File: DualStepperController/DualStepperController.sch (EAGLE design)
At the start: 14 parts

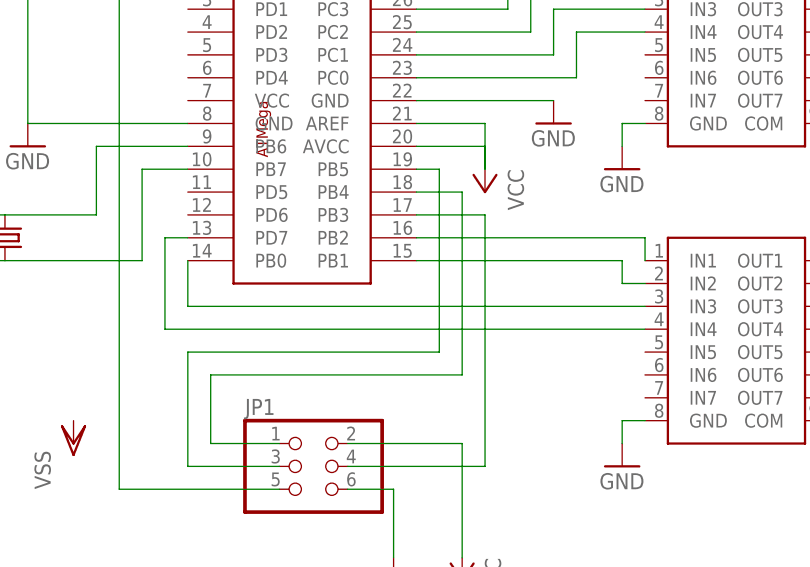
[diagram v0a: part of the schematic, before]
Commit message: Add mounting holes.
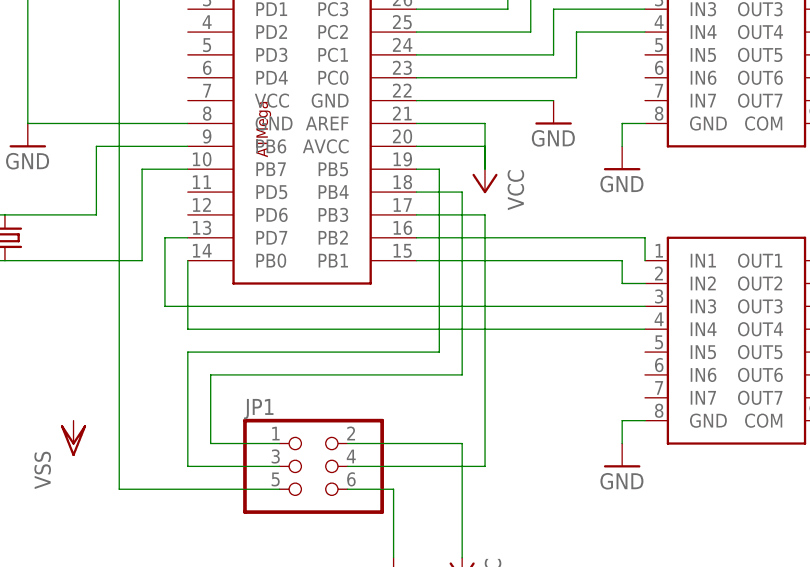
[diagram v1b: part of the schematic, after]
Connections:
- net N$24: now also U$3.IN4; no longer U$3.IN3
- net N$25: now also U$3.IN3; no longer U$3.IN4
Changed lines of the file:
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@@
 <grid distance="0.1" unitdist="inch" unit="inch" style="lines" multiple="1" display="no" altdistance="0.01" altunitdist="inch" altunit="inch"/>
 <layers>
-<layer number="1" name="Top" color="4" fill="1" visible="yes" active="no"/>
-<layer number="16" name="Bottom" color="1" fill="1" visible="yes" active="no"/>
-<layer number="17" name="Pads" color="2" fill="1" visible="yes" active="no"/>
-<layer number="18" name="Vias" color="2" fill="1" visible="yes" active="no"/>
-<layer number="19" name="Unrouted" color="6" fill="1" visible="yes" active="no"/>
-<layer number="20" name="Dimension" color="15" fill="1" visible="yes" active="no"/>
-<layer number="21" name="tPlace" color="7" fill="1" visible="yes" active="no"/>
-<layer number="22" name="bPlace" color="7" fill="1" visible="yes" active="no"/>
-<layer number="23" name="tOrigins" color="15" fill="1" visible="yes" active="no"/>
-<layer number="24" name="bOrigins" color="15" fill="1" visible="yes" active="no"/>
-<layer number="25" name="tNames" color="7" fill="1" visible="yes" active="no"/>
-<layer number="26" name="bNames" color="7" fill="1" visible="yes" active="no"/>
-<layer number="27" name="tValues" color="7" fill="1" visible="yes" active="no"/>
-<layer number="28" name="bValues" color="7" fill="1" visible="yes" active="no"/>
+<layer number="1" name="Top" color="4" fill="1" visible="no" active="no"/>
+<layer number="16" name="Bottom" color="1" fill="1" visible="no" active="no"/>
+<layer number="17" name="Pads" color="2" fill="1" visible="no" active="no"/>
+<layer number="18" name="Vias" color="2" fill="1" visible="no" active="no"/>
+<layer number="19" name="Unrouted" color="6" fill="1" visible="no" active="no"/>
+<layer number="20" name="Dimension" color="15" fill="1" visible="no" active="no"/>
+<layer number="21" name="tPlace" color="7" fill="1" visible="no" active="no"/>
+<layer number="22" name="bPlace" color="7" fill="1" visible="no" active="no"/>
+<layer number="23" name="tOrigins" color="15" fill="1" visible="no" active="no"/>
+<layer number="24" name="bOrigins" color="15" fill="1" visible="no" active="no"/>
+<layer number="25" name="tNames" color="7" fill="1" visible="no" active="no"/>
+<layer number="26" name="bNames" color="7" fill="1" visible="no" active="no"/>
+<layer number="27" name="tValues" color="7" fill="1" visible="no" active="no"/>
+<layer number="28" name="bValues" color="7" fill="1" visible="no" active="no"/>
 <layer number="29" name="tStop" color="7" fill="3" visible="no" active="no"/>
 <layer number="30" name="bStop" color="7" fill="6" visible="no" active="no"/>
@@
 <layer number="35" name="tGlue" color="7" fill="4" visible="no" active="no"/>
 <layer number="36" name="bGlue" color="7" fill="5" visible="no" active="no"/>
-<layer number="37" name="tTest" color="7" fill="1" visible="yes" active="no"/>
-<layer number="38" name="bTest" color="7" fill="1" visible="yes" active="no"/>
+<layer number="37" name="tTest" color="7" fill="1" visible="no" active="no"/>
+<layer number="38" name="bTest" color="7" fill="1" visible="no" active="no"/>
 <layer number="39" name="tKeepout" color="4" fill="11" visible="no" active="no"/>
 <layer number="40" name="bKeepout" color="1" fill="11" visible="no" active="no"/>
@@
 <layer number="44" name="Drills" color="7" fill="1" visible="no" active="no"/>
 <layer number="45" name="Holes" color="7" fill="1" visible="no" active="no"/>
-<layer number="46" name="Milling" color="3" fill="1" visible="yes" active="no"/>
-<layer number="47" name="Measures" color="7" fill="1" visible="yes" active="no"/>
-<layer number="48" name="Document" color="7" fill="1" visible="yes" active="no"/>
-<layer number="49" name="Reference" color="7" fill="1" visible="yes" active="no"/>
-<layer number="51" name="tDocu" color="7" fill="1" visible="yes" active="no"/>
-<layer number="52" name="bDocu" color="7" fill="1" visible="yes" active="no"/>
+<layer number="46" name="Milling" color="3" fill="1" visible="no" active="no"/>
+<layer number="47" name="Measures" color="7" fill="1" visible="no" active="no"/>
+<layer number="48" name="Document" color="7" fill="1" visible="no" active="no"/>
+<layer number="49" name="Reference" color="7" fill="1" visible="no" active="no"/>
+<layer number="51" name="tDocu" color="7" fill="1" visible="no" active="no"/>
+<layer number="52" name="bDocu" color="7" fill="1" visible="no" active="no"/>
 <layer number="90" name="Modules" color="5" fill="1" visible="yes" active="yes"/>
 <layer number="91" name="Nets" color="2" fill="1" visible="yes" active="yes"/>
@@
 <segment>
 <pinref part="U$1" gate="G$1" pin="PB0"/>
-<pinref part="U$3" gate="G$1" pin="IN3"/>
-<wire x1="30.48" y1="38.1" x2="30.48" y2="33.02" width="0.1524" layer="91"/>
-<wire x1="30.48" y1="33.02" x2="81.28" y2="33.02" width="0.1524" layer="91"/>
+<wire x1="30.48" y1="38.1" x2="30.48" y2="30.48" width="0.1524" layer="91"/>
+<pinref part="U$3" gate="G$1" pin="IN4"/>
+<wire x1="30.48" y1="30.48" x2="81.28" y2="30.48" width="0.1524" layer="91"/>
 </segment>
 </net>
@@
 <pinref part="U$1" gate="G$1" pin="PD7"/>
 <wire x1="30.48" y1="40.64" x2="27.94" y2="40.64" width="0.1524" layer="91"/>
-<wire x1="27.94" y1="40.64" x2="27.94" y2="30.48" width="0.1524" layer="91"/>
-<pinref part="U$3" gate="G$1" pin="IN4"/>
-<wire x1="27.94" y1="30.48" x2="81.28" y2="30.48" width="0.1524" layer="91"/>
-</segment>
-</net>
+<wire x1="27.94" y1="40.64" x2="27.94" y2="33.02" width="0.1524" layer="91"/>
+<pinref part="U$3" gate="G$1" pin="IN3"/>
+<wire x1="27.94" y1="33.02" x2="81.28" y2="33.02" width="0.1524" layer="91"/>
+</segment>
+</net>

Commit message: Add serial header to Dual Stepper Controller. Add a new project for a ESP breakout board.
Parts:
- added SER: (no value), pinhead:PINHD-1X3
- R1: device rcl:R-US_0411/12 -> rcl:R-US_0207/7
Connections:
- new net N$13: SER.1, U$1.PD1
- new net N$26: SER.2, U$1.PD0
- net GND: now also SER.3
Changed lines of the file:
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@@
 <part name="I2CIN" library="pinhead" deviceset="PINHD-1X3" device=""/>
 <part name="VSS1" library="supply1" deviceset="VSS" device=""/>
-<part name="VSS2" library="supply1" deviceset="VSS" device=""/>
 <part name="GND1" library="supply1" deviceset="GND" device=""/>
 <part name="GND2" library="supply1" deviceset="GND" device=""/>
@@
 <part name="C2" library="rcl" deviceset="C-US" device="025-024X044"/>
 <part name="GND5" library="supply1" deviceset="GND" device=""/>
-<part name="R1" library="rcl" deviceset="R-US_" device="0411/12" value="10k"/>
+<part name="R1" library="rcl" deviceset="R-US_" device="0207/7" value="10k"/>
 <part name="P+1" library="supply1" deviceset="VCC" device=""/>
 <part name="JP1" library="pinhead" deviceset="PINHD-2X3" device=""/>
@@
 <part name="VSS" library="solpad" deviceset="SE14" device=""/>
 <part name="GND" library="solpad" deviceset="SE14" device=""/>
+<part name="SER" library="pinhead" deviceset="PINHD-1X3" device=""/>
 </parts>
 <sheets>
@@
 <instance part="I2CIN" gate="A" x="2.54" y="88.9" rot="R180"/>
 <instance part="VSS1" gate="G$1" x="134.62" y="15.24"/>
-<instance part="VSS2" gate="G$1" x="17.78" y="17.78"/>
 <instance part="GND1" gate="1" x="78.74" y="48.26"/>
 <instance part="GND2" gate="1" x="78.74" y="15.24"/>
@@
 <instance part="VSS" gate="1" x="78.74" y="101.6"/>
 <instance part="GND" gate="1" x="101.6" y="83.82" rot="R270"/>
+<instance part="SER" gate="A" x="2.54" y="68.58" rot="R180"/>
 </instances>
 <busses>
@@
 <pinref part="I2CIN" gate="A" pin="1"/>
 <wire x1="5.08" y1="86.36" x2="12.7" y2="86.36" width="0.1524" layer="91"/>
-<wire x1="12.7" y1="86.36" x2="12.7" y2="53.34" width="0.1524" layer="91"/>
+<wire x1="12.7" y1="86.36" x2="12.7" y2="71.12" width="0.1524" layer="91"/>
 <pinref part="GND3" gate="1" pin="GND"/>
 <pinref part="U$1" gate="G$1" pin="GND@1"/>
+<wire x1="12.7" y1="71.12" x2="12.7" y2="53.34" width="0.1524" layer="91"/>
 <wire x1="12.7" y1="53.34" x2="30.48" y2="53.34" width="0.1524" layer="91"/>
+<pinref part="SER" gate="A" pin="3"/>
+<wire x1="5.08" y1="71.12" x2="12.7" y2="71.12" width="0.1524" layer="91"/>
 </segment>
 <segment>
@@
 </segment>
 </net>
+<net name="N$13" class="0">
+<segment>
+<pinref part="SER" gate="A" pin="1"/>
+<pinref part="U$1" gate="G$1" pin="PD1"/>
+<wire x1="5.08" y1="66.04" x2="30.48" y2="66.04" width="0.1524" layer="91"/>
+</segment>
+</net>
+<net name="N$26" class="0">
+<segment>
+<pinref part="U$1" gate="G$1" pin="PD0"/>
+<pinref part="SER" gate="A" pin="2"/>
+<wire x1="30.48" y1="68.58" x2="5.08" y2="68.58" width="0.1524" layer="91"/>
+</segment>
+</net>
